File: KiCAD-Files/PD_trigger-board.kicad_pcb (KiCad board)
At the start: 2 copper layers, 18 x 23.5 mm, 16 parts, among them J1 USB_C_Receptacle_USB3.0_12P, U1 HUSB238, U2 SIR1309DP, U3 ESP32-S3-mini_pinprofile

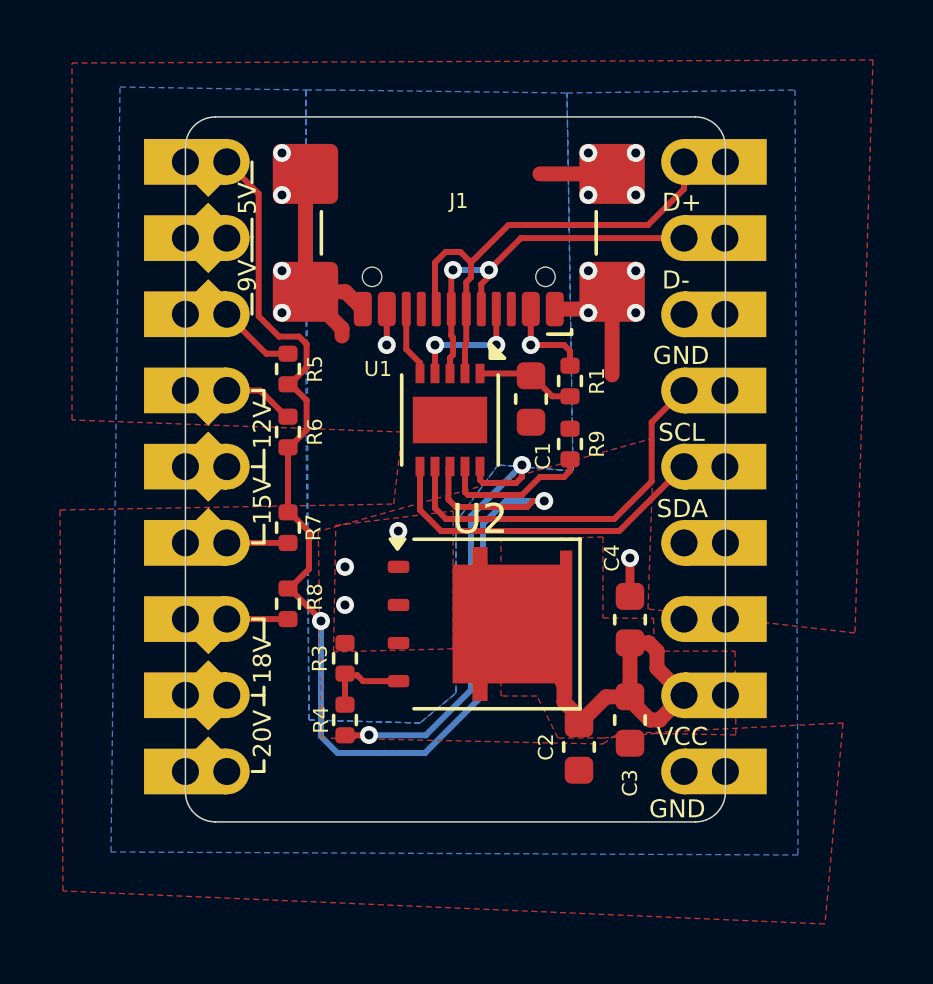
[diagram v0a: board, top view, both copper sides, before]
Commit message: thermal relief deleted
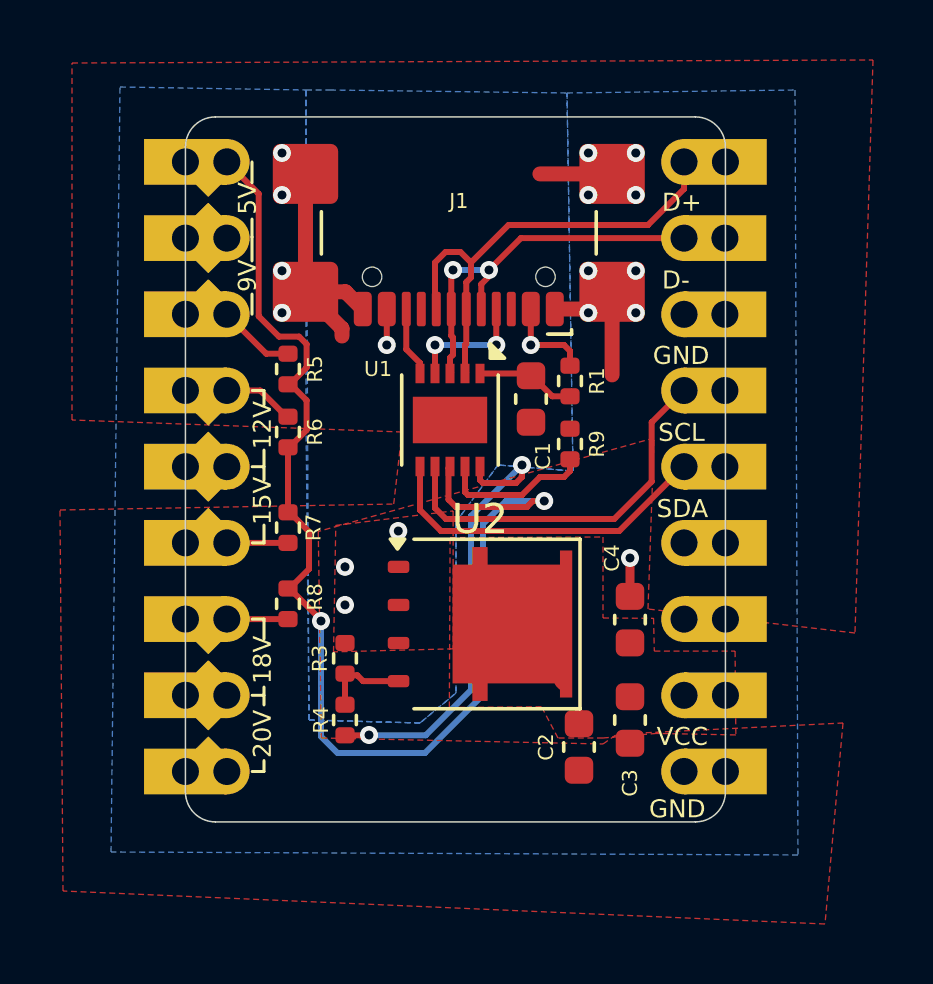
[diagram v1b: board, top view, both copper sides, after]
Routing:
- net VOUT: track 11.3 -> 0.87 mm
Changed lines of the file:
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@@
-	)
-	(segment
-		(start 144.2 96.1)
-		(end 143.7 95.6)
-		(width 0.5)
-		(layer "F.Cu")
-		(net 2)
 	)
 	(segment
@@
 	)
 	(segment
-		(start 144.2 96.325)
-		(end 145.0972 95.4278)
-		(width 0.5)
-		(layer "F.Cu")
-		(net 2)
-	)
-	(segment
 		(start 145.72546 93.635)
 		(end 145.72069 93.63023)
@@
 	)
 	(segment
-		(start 145.9 95.539172)
-		(end 146.560828 96.2)
-		(width 0.5)
-		(layer "F.Cu")
-		(net 2)
-	)
-	(segment
 		(start 145.9 93.63023)
 		(end 145.73023 93.63023)
@@
 	)
 	(segment
-		(start 143.7 95.6)
-		(end 143.7 94.98085)
-		(width 0.5)
-		(layer "F.Cu")
-		(net 2)
-	)
-	(segment
-		(start 145.0972 95.4278)
-		(end 145.8972 95.4278)
-		(width 0.5)
-		(layer "F.Cu")
-		(net 2)
-	)
-	(segment
-		(start 146.9 96.178)
-		(end 147.701 95.377)
-		(width 0.5)
-		(layer "F.Cu")
-		(net 2)
-	)
-	(segment
-		(start 146.8 93.9)
-		(end 146.8 94.476)
-		(width 0.5)
-		(layer "F.Cu")
-		(net 2)
-	)
-	(segment
-		(start 146.53023 93.63023)
-		(end 146.8 93.9)
-		(width 0.5)
-		(layer "F.Cu")
-		(net 2)
-	)
-	(segment
 		(start 145.95423 93.63023)
 		(end 145.9 93.63023)
@@
 	)
 	(segment
-		(start 146.8 94.476)
-		(end 147.701 95.377)
-		(width 0.5)
-		(layer "F.Cu")
-		(net 2)
-	)
-	(segment
 		(start 145.9 95.125)
 		(end 145.9 95.3)
@@
 	)
 	(segment
-		(start 146.9 96.2)
-		(end 146.9 96.178)
-		(width 0.5)
-		(layer "F.Cu")
-		(net 2)
-	)
-	(segment
-		(start 145.9 95.425)
-		(end 145.9 93.63023)
-		(width 0.5)
-		(layer "F.Cu")
-		(net 2)
-	)
-	(segment
 		(start 145.9 95.425)
 		(end 145.9 95.539172)
-		(width 0.5)
-		(layer "F.Cu")
-		(net 2)
-	)
-	(segment
-		(start 145.9 93.63023)
-		(end 146.53023 93.63023)
-		(width 0.5)
-		(layer "F.Cu")
-		(net 2)
-	)
-	(segment
-		(start 146.560828 96.2)
-		(end 146.9 96.2)
 		(width 0.5)
 		(layer "F.Cu")
@@
 		(layer "F.Cu")
 		(hatch edge 0.5)
-		(connect_pads
+		(connect_pads yes
 			(clearance 0.5)
 		)
@@
 		(polygon
 			(pts
-				(xy 149.4282 96.6978) (xy 146.7866 96.647) (xy 145 96.8) (xy 143.5 96.8) (xy 142.8 95.4) (xy 141.6 95.4)
-				(xy 141.6 90.2) (xy 145 90.1) (xy 145 92.8) (xy 146.685 92.8116) (xy 146.7104 93.9038) (xy 149.4028 93.9038)
+				(xy 149.4282 96.6978) (xy 146.7866 96.647) (xy 145 96.8) (xy 143.5 96.8) (xy 142.9512 95.758) (xy 139.8778 95.7834)
+				(xy 139.9032 90.1192) (xy 145 90.1) (xy 145 92.8) (xy 146.685 92.8116) (xy 146.7104 93.9038) (xy 149.4028 93.9038)
 			)
 		)
@@
 		(hatch edge 0.5)
 		(priority 4)
-		(connect_pads
+		(connect_pads yes
 			(clearance 0.5)
 		)

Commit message: changed version number. added ce and weee symbol
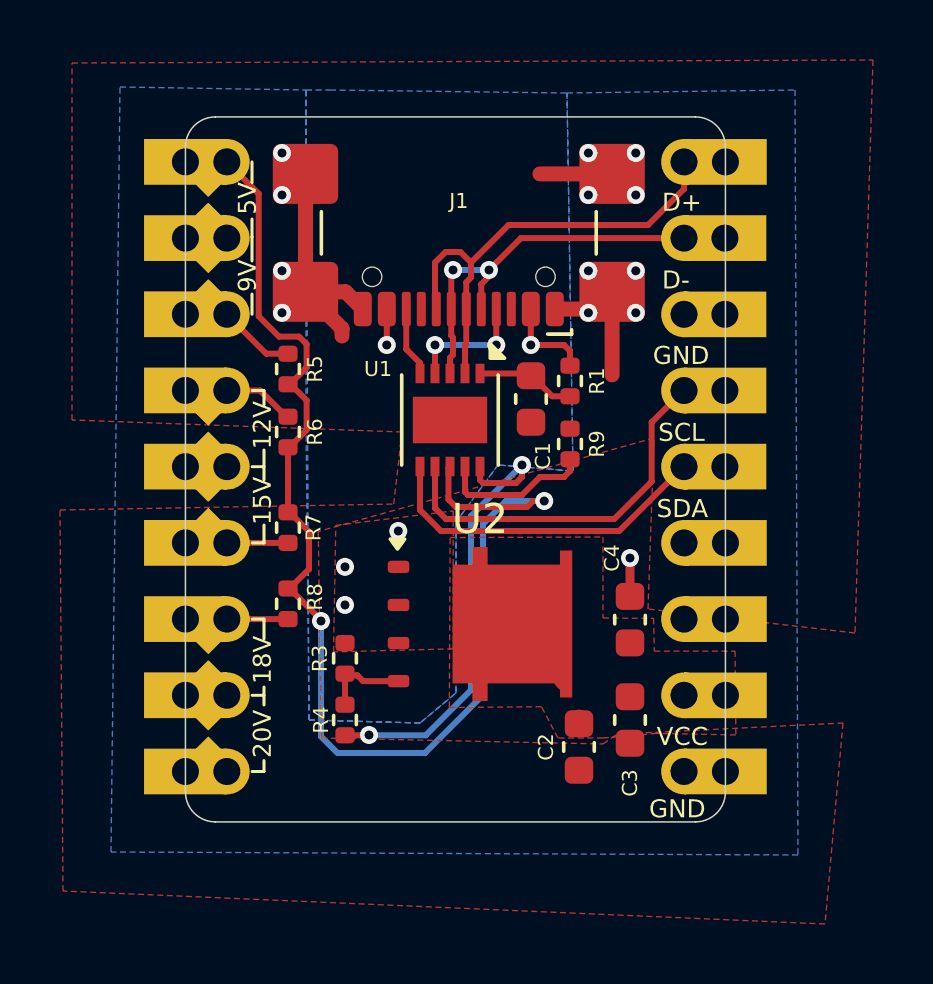
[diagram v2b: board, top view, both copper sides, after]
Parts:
- added ce_icon_SilkS_3mm: G***, blinkyparts:ce-icon_SilkS_3mm, B.Cu at (143.1, 77.5)
- added weee-icon_SilkS_3mm: G***, blinkyparts:weee-icon_SilkS_3mm, B.Cu at (138.8, 77.4)
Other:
- board text added: "v0.3"
- board text removed: "v0.2"

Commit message: placed diodes and minor design changes
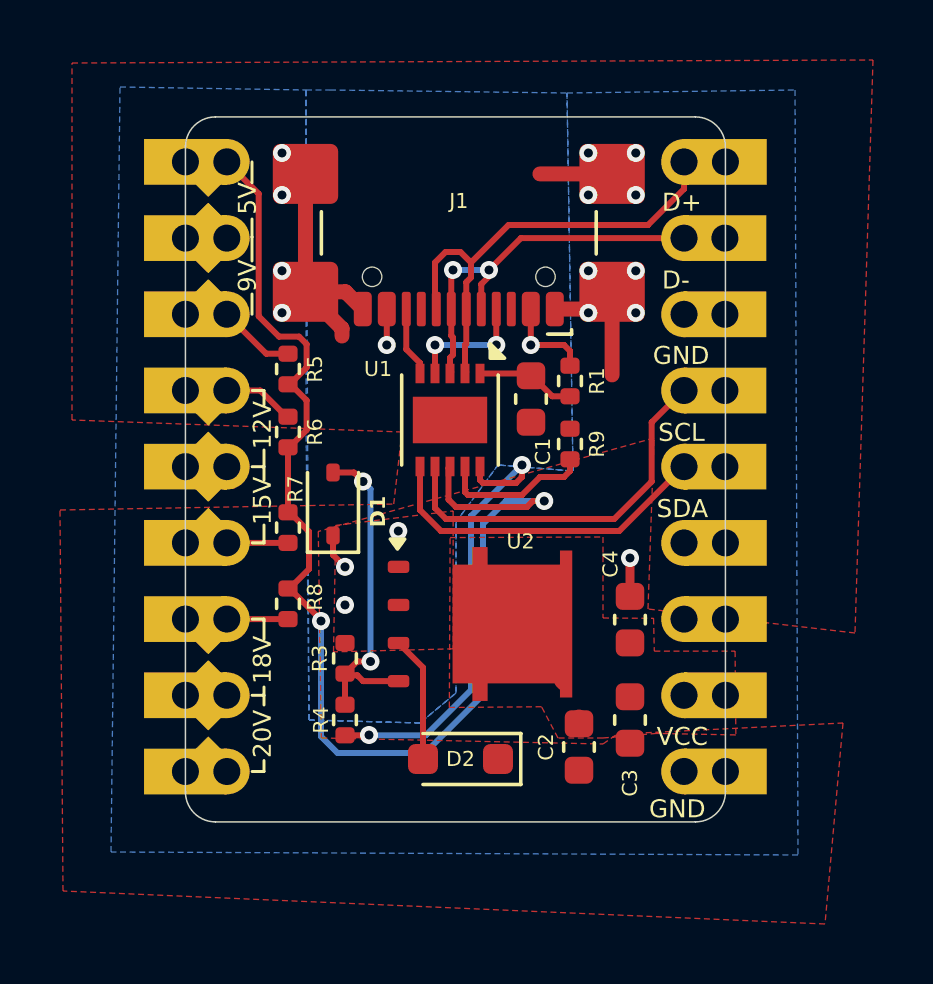
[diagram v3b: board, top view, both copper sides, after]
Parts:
- added D1: D_Zener, Diode_SMD:D_SOD-323, F.Cu at (136.0, 89.0)
- added D2: SD15_SOD323, Diode_SMD:D_SOD-323_HandSoldering, F.Cu at (140.2, 97.5)
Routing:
- net Net-(D1-A): track 2.84 -> 11.1 mm, vias 0 -> 2
- net VBUS: track 4.29 -> 9.70 mm
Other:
- board text added: "PD-Trigger-Board PD 3.0 v0.4"
- board text added: "blinkyparts GmbH Egerstr. 9, RGB CC-BY-NC-SA 4.0"
- board text removed: "PD-Trigger-Board PD 3.0"
- board text removed: "blinkyparts GmbH Egerstr. 9, RGB CC-BY-SA 4.0"
- board text removed: "v0.3"
